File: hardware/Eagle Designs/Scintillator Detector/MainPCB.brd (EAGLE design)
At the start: 90.2 x 95.9 mm, 32 parts, among them J1 503763-0591, J4 503763-0591, U1 LT1807IS8PBF, U2 LT3461AES6TRMPBF, U3 TMP36GSZ

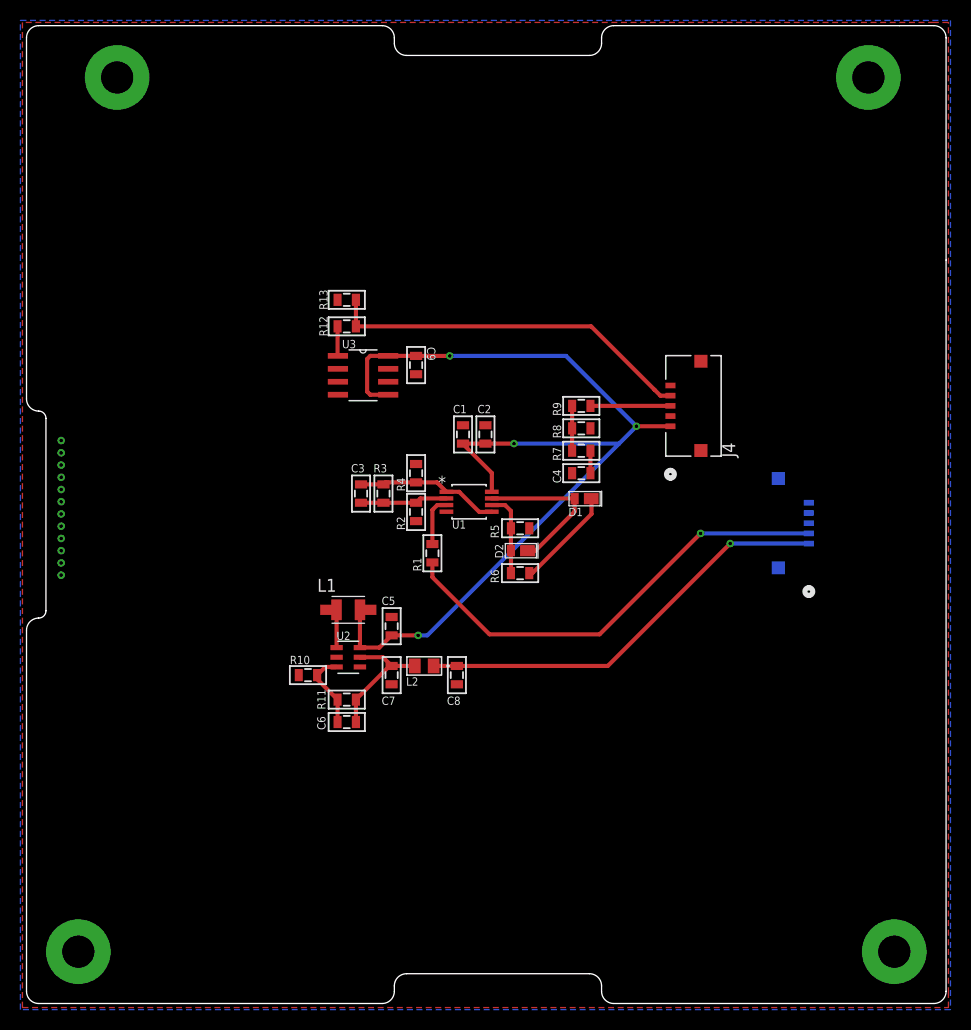
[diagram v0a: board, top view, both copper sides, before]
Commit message: Updated scintillator detector PCB
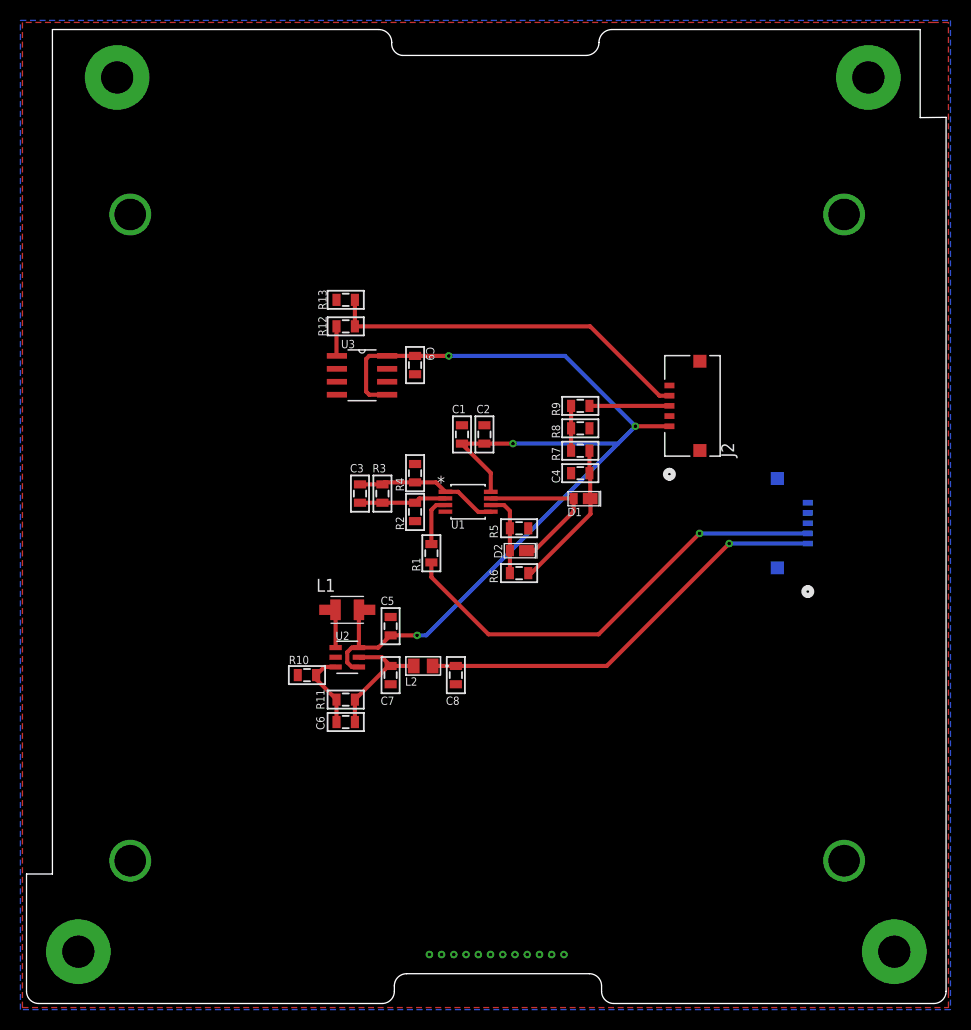
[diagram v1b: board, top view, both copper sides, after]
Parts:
- removed J4: 503763-0591, Molex - 503763-0591:CONN_5037630591_MOL
- added J2: 503763-0591, Molex - 503763-0591:CONN_5037630591_MOL
- U$1: value PC104 -> PC104_WCONN_DETECTOR; device HSFL_Main_Library:PC104 -> HSFL_Main_Library:PC104_WCONN_DETECTOR
- moved J1 0.10 mm to (74.3, 47.1)
- moved C2 0.10 mm to (44.9, 55.8)
- moved C4 0.10 mm to (54.3, 52.0)
- moved C8 0.10 mm to (42.1, 32.2)
- moved C9 0.10 mm to (38.1, 62.6)
- moved D1 0.10 mm to (54.3, 49.5)
- moved D2 0.10 mm to (48.0, 44.4)
- moved L1 0.10 mm to (31.4, 38.6)
- moved L2 0.10 mm to (38.9, 33.1)
- moved R10 0.10 mm to (27.5, 32.2)
- moved R2 0.10 mm to (38.1, 48.2)
- moved R3 0.10 mm to (34.9, 50.0)
- moved R4 0.10 mm to (38.1, 52.0)
- moved R5 0.10 mm to (48.3, 46.6)
- moved R6 0.10 mm to (48.3, 42.2)
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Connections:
- net 5V: now also J2.1; no longer J4.1
- net GND: now also J2.2, J2.5, J2.6, J2.7; no longer J4.2, J4.5, J4.6, J4.7
- net RASPI_SIG: now also J2.3; no longer J4.3
- net TMP_DATA: now also J2.4; no longer J4.4
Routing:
- net 5V: track 99.2 -> 102.8 mm
- net N$5: track 12.3 -> 14.7 mm
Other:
- board size 90.2 x 95.9 mm -> 90.2 x 95.5 mm

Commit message: Updated temp sensor circuit for scintillator pcb
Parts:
- R12: value 27k -> 45.3k
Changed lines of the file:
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@@
 <attribute name="NAME" x="30.839040625" y="64.253440625" size="0.8128" layer="25" ratio="10" rot="SR0"/>
 </element>
-<element name="R12" library="HSFL_Main_Library" package="0805" value="27k" x="31.3" y="66.4" smashed="yes" rot="R180">
+<element name="R12" library="HSFL_Main_Library" package="0805" value="45.3k" x="31.3" y="66.4" smashed="yes" rot="R180">
 <attribute name="NAME" x="29.4205" y="65.422" size="0.8128" layer="25" font="vector" ratio="15" rot="SR90"/>
 </element>

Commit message: Changed scintillator temp sensor
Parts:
- U3: value TMP36GSZ -> TMP36FSZ
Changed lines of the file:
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@@
 <attribute name="NAME" x="29.2205" y="28.822" size="0.8128" layer="25" font="vector" ratio="15" rot="SR90"/>
 </element>
-<element name="U3" library="TMP36GSZ" package="SOIC127P600X175-8N" value="TMP36GSZ" x="32.9" y="61.6" smashed="yes">
+<element name="U3" library="TMP36GSZ" package="SOIC127P600X175-8N" value="TMP36FSZ" x="32.9" y="61.6" smashed="yes">
 <attribute name="NAME" x="30.839040625" y="64.253440625" size="0.8128" layer="25" ratio="10" rot="SR0"/>
 </element>

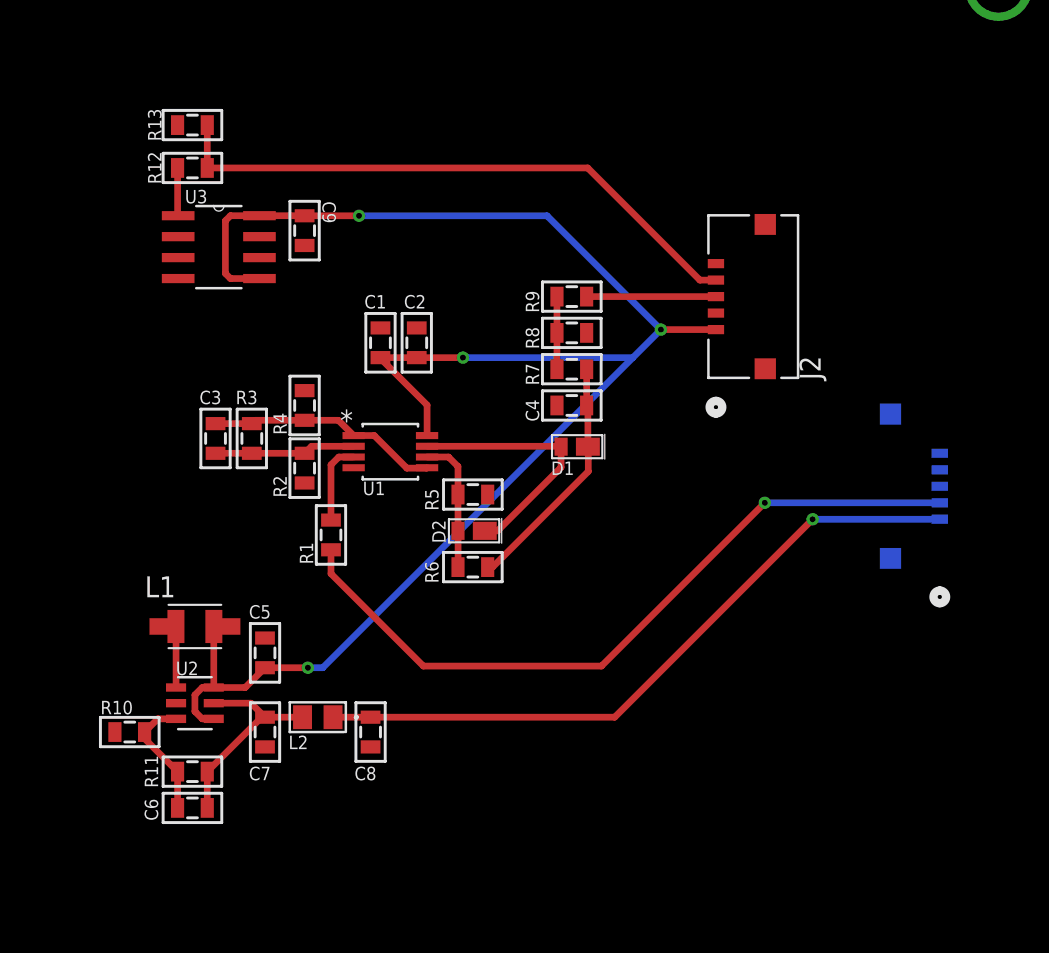
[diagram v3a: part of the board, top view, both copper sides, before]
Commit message: Scintillator detector edits
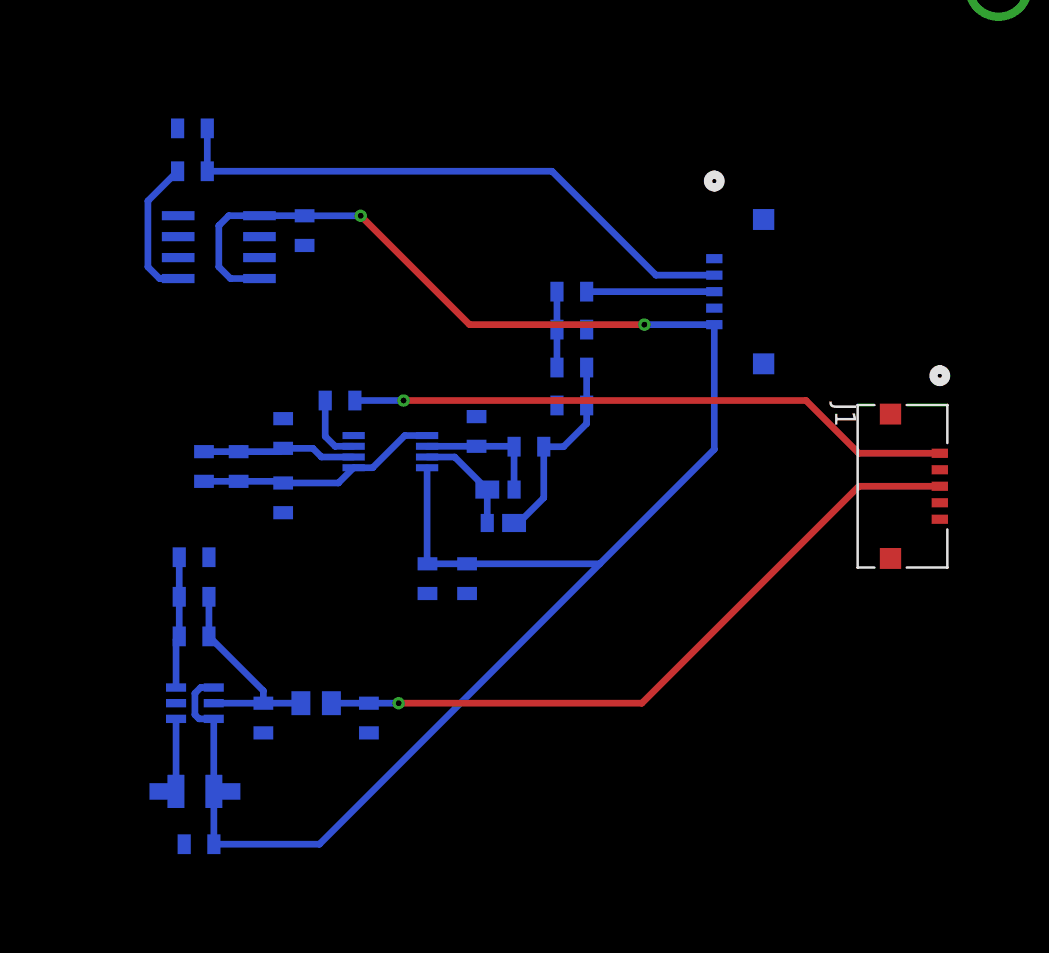
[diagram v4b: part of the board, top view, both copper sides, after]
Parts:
- moved C2 14.6 mm to (48.0, 41.5), flipped to the bottom, turned to 90 degrees
- moved C1 14.6 mm to (45.5, 41.5), flipped to the bottom, turned to 90 degrees
- moved C5 12.3 mm to (31.7, 25.4), flipped to the bottom, turned to 180 degrees
- moved R10 11.3 mm to (31.4, 42.8), flipped to the bottom
- moved R11 10.6 mm to (31.4, 40.4), flipped to the bottom, turned to 180 degrees
- moved C6 10.4 mm to (31.4, 38.0), flipped to the bottom, turned to 180 degrees
- moved L1 10.0 mm to (31.4, 28.6), flipped to the bottom, turned to 180 degrees
- moved R1 8.17 mm to (40.2, 52.3), flipped to the bottom, turned to 0 degrees
- moved R6 8.05 mm to (51.7, 49.5), flipped to the bottom, turned to 180 degrees
- moved D1 6.44 mm to (49.8, 44.9), flipped to the bottom, turned to 180 degrees
- moved R4 5.75 mm to (36.8, 46.4), flipped to the bottom, turned to 270 degrees
- moved R5 3.83 mm to (48.5, 50.4), flipped to the bottom, turned to 270 degrees
- moved D2 3.26 mm to (50.1, 46.9), flipped to the bottom
- moved R2 2.47 mm to (36.8, 50.3), flipped to the bottom, turned to 270 degrees
- moved R3 1.88 mm to (34.1, 48.3), flipped to the bottom, turned to 270 degrees
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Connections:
- net 5V: now also J2.5; no longer J2.1
- net GND: now also J1.2, J2.1, J2.4; no longer J1.3, J2.2, J2.5
- net SIPM_PWR: now also J1.3; no longer J1.1
- net SIPM_SIG: now also J1.1; no longer J1.2
- net TMP_DATA: now also J2.2; no longer J2.4
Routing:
- net 5V: track 102.8 -> 113.8 mm, vias 4 -> 2
- net N$6: track 15.6 -> 6.49 mm
- net SIPM_SIG: track 44.8 -> 36.8 mm
- net N$11: track 2.91 -> 8.67 mm
- net N$5: track 14.7 -> 12.1 mm
- net N$2: track 8.55 -> 9.66 mm
- net OUTA: track 14.1 -> 14.9 mm
- net N$1: track 4.92 -> 4.15 mm
- net N$8: track 3.70 -> 4.40 mm
- net SIPM_PWR: track 41.8 -> 42.3 mm
